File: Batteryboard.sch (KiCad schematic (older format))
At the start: 150 parts, among them IC1 FAN4010IL6X_F113, IC2 FAN4010IL6X_F113, IC3 FAN4010IL6X_F113, J1 Conn_01x02_Male, J2 Conn_01x03_Male, J3 Conn_01x05_Male, J4 Conn_01x02_Male, J5 SC_19-20, Q1 SI7617DN-T1-GE3, Q2 SI7617DN-T1-GE3, Q3 SI7617DN-T1-GE3, Q4 SIS412DN-T1-GE3, Q5 SIS412DN-T1-GE3, Q6 SIS412DN-T1-GE3, Q7 SI7617DN-T1-GE3, Q8 SIS412DN-T1-GE3, U1 BQ24617RGET, U2 TPS65279DAPR, U3 BQ29200DRBT, U4 PIC18F25K50-I_SO, U5 MCP2515-xSO, U6 SN65HVD1050D

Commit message: schematic is final now, working on routing my board again
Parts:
- C47: footprint Capacitor_SMD:C_0603_1608Metric -> Capacitor_SMD:C_0805_2012Metric
- IC1, IC2, IC3: symbol Batteryboard-rescue:FAN4010IL6X_F113-FAN4010IL6X_F113 -> FAN4010IL6X_F113:FAN4010IL6X_F113
- J1, J4: footprint Connector_JST:JST_VH_B2PS-VH_1x02_P3.96mm_Horizontal -> 1-1123723-2:1-1123723-2
- TMP1: symbol Batteryboard-rescue:LM50CIM3X-MASA-LIB -> MASA-LIB:LM50CIM3X
- U2: symbol Batteryboard-rescue:TPS65279DAPR-TPS65279DAPR -> TPS65279DAPR:TPS65279DAPR
- U4: symbol Batteryboard-rescue:PIC18F25K50-I_SO-PIC18F25K50-ISO -> PIC18F25K50-ISO:PIC18F25K50-I_SO
- gave numbers to parts that had none: 8
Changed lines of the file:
@@
 F 0 "J1" H 1308 4131 50  0000 C CNN
 F 1 "Conn_01x02_Male" H 1308 4040 50  0000 C CNN
-F 2 "Connector_JST:JST_VH_B2PS-VH_1x02_P3.96mm_Horizontal" H 1200 3950 50  0001 C CNN
+F 2 "1-1123723-2:1-1123723-2" H 1200 3950 50  0001 C CNN
 F 3 "~" H 1200 3950 50  0001 C CNN
 	1    1200 3950
@@
 F 0 "J4" H 10358 4781 50  0000 C CNN
 F 1 "Conn_01x02_Male" H 10358 4690 50  0000 C CNN
-F 2 "Connector_JST:JST_VH_B2PS-VH_1x02_P3.96mm_Horizontal" H 10250 4600 50  0001 C CNN
+F 2 "1-1123723-2:1-1123723-2" H 10250 4600 50  0001 C CNN
 F 3 "~" H 10250 4600 50  0001 C CNN
 	1    10250 4600
@@
 F 0 "C47" H 16115 7646 50  0000 L CNN
 F 1 "33uF" H 16115 7555 50  0000 L CNN
-F 2 "Capacitor_SMD:C_0603_1608Metric" H 16038 7450 50  0001 C CNN
+F 2 "Capacitor_SMD:C_0805_2012Metric" H 16038 7450 50  0001 C CNN
 F 3 "~" H 16000 7600 50  0001 C CNN
 	1    16000 7600
@@
 FB2
 $Comp
-L Batteryboard-rescue:FAN4010IL6X_F113-FAN4010IL6X_F113 IC2
+L FAN4010IL6X_F113:FAN4010IL6X_F113 IC2
 U 1 1 5E16FEE4
 P 11250 9300
@@
 	-1   0    0    -1
 $EndComp
-$Comp
-L Batteryboard-rescue:FAN4010IL6X_F113-FAN4010IL6X_F113 IC3
-U 1 1 5E16B258
-P 15800 8550
-F 0 "IC3" H 16350 8815 50  0000 C CNN
-F 1 "FAN4010IL6X_F113" H 16350 8724 50  0000 C CNN
-F 2 "MASA-LIB:6-LEAD_MICROPAK" H 16750 8650 50  0001 L CNN
-F 3 "http://pdl.designspark.com/api/v1/manufacturers/53f31bb99b4759f8698ebd6d/part/54f601839b4759c27e8ce92c/54f601849b4759c27e8ce954/1pdf" H 16750 8550 50  0001 L CNN
-F 4 "Current Sense Amplifier Single Single Ended 6-Pin MLP" H 16750 8450 50  0001 L CNN "Description"
-F 5 "" H 16750 8350 50  0001 L CNN "Height"
-F 6 "ON Semiconductor" H 16750 8250 50  0001 L CNN "Manufacturer_Name"
-F 7 "FAN4010IL6X_F113" H 16750 8150 50  0001 L CNN "Manufacturer_Part_Number"
-F 8 "512-FAN4010IL6X_F113" H 16750 8050 50  0001 L CNN "Mouser Part Number"
-F 9 "http://www.mouser.com/Search/ProductDetail.aspx?qs=bXpVsf6NmSLCEHlKPwERMg%3d%3d" H 16750 7950 50  0001 L CNN "Mouser Price/Stock"
-F 10 "8650874P" H 16750 7850 50  0001 L CNN "RS Part Number"
-F 11 "http://uk.rs-online.com/web/p/products/8650874P" H 16750 7750 50  0001 L CNN "RS Price/Stock"
-	1    15800 8550
-	1    0    0    -1
-$EndComp
 Text Notes 3950 8850 1    50   ~ 0
 make this guy give 3.6V so half the input
@@
 Wire Wire Line
 	12450 7900 12250 7900
-$Comp
-L Batteryboard-rescue:TPS65279DAPR-TPS65279DAPR U2
-U 1 1 5E217675
-P 12500 7000
-F 0 "U2" H 13400 7387 60  0000 C CNN
-F 1 "TPS65279DAPR" H 13400 7281 60  0000 C CNN
-F 2 "TPS65279DAPR:TPS65279DAPR" H 13400 7240 60  0001 C CNN
-F 3 "" H 12500 7000 60  0000 C CNN
-	1    12500 7000
-	1    0    0    -1
-$EndComp
 Wire Wire Line
 	13750 10050 13650 10050
@@
 	12500 7800 12450 7800
 $Comp
-L Batteryboard-rescue:LM50CIM3X-MASA-LIB TMP1
+L MASA-LIB:LM50CIM3X TMP1
 U 1 1 5E0BF102
 P 15000 9900
@@
 PGC
 $Comp
-L Batteryboard-rescue:PIC18F25K50-I_SO-PIC18F25K50-ISO U4
+L PIC18F25K50-ISO:PIC18F25K50-I_SO U4
 U 1 1 5EEDA796
 P 5000 8000
@@
 7.4V LINE
 $Comp
-L Batteryboard-rescue:FAN4010IL6X_F113-FAN4010IL6X_F113 IC1
-U 1 1 5E171494
-P 10100 1650
-F 0 "IC1" H 10650 1915 50  0000 C CNN
-F 1 "FAN4010IL6X_F113" H 10650 1824 50  0000 C CNN
-F 2 "MASA-LIB:6-LEAD_MICROPAK" H 11050 1750 50  0001 L CNN
-F 3 "http://pdl.designspark.com/api/v1/manufacturers/53f31bb99b4759f8698ebd6d/part/54f601839b4759c27e8ce92c/54f601849b4759c27e8ce954/1pdf" H 11050 1650 50  0001 L CNN
-F 4 "Current Sense Amplifier Single Single Ended 6-Pin MLP" H 11050 1550 50  0001 L CNN "Description"
-F 5 "" H 11050 1450 50  0001 L CNN "Height"
-F 6 "ON Semiconductor" H 11050 1350 50  0001 L CNN "Manufacturer_Name"
-F 7 "FAN4010IL6X_F113" H 11050 1250 50  0001 L CNN "Manufacturer_Part_Number"
-F 8 "512-FAN4010IL6X_F113" H 11050 1150 50  0001 L CNN "Mouser Part Number"
-F 9 "http://www.mouser.com/Search/ProductDetail.aspx?qs=bXpVsf6NmSLCEHlKPwERMg%3d%3d" H 11050 1050 50  0001 L CNN "Mouser Price/Stock"
-F 10 "8650874P" H 11050 950 50  0001 L CNN "RS Part Number"
-F 11 "http://uk.rs-online.com/web/p/products/8650874P" H 11050 850 50  0001 L CNN "RS Price/Stock"
-	1    10100 1650
-	1    0    0    1
-$EndComp
-$Comp
 L power:GNDREF #PWR0119
 U 1 1 5E267823
@@
 $EndComp
 $Comp
-L Device:C C?
+L Device:C C23
 U 1 1 5E428FCB
 P 14200 10050
-F 0 "C?" V 13948 10050 50  0000 C CNN
+F 0 "C23" V 13948 10050 50  0000 C CNN
 F 1 "1nF" V 14039 10050 50  0000 C CNN
 F 2 "Capacitor_SMD:C_0603_1608Metric" H 14238 9900 50  0001 C CNN
@@
 $EndComp
 $Comp
-L Device:C C?
+L Device:C C31
 U 1 1 5E429589
 P 14400 10050
-F 0 "C?" V 14148 10050 50  0000 C CNN
+F 0 "C31" V 14148 10050 50  0000 C CNN
 F 1 "100nF" V 14239 10050 50  0000 C CNN
 F 2 "Capacitor_SMD:C_0603_1608Metric" H 14438 9900 50  0001 C CNN
@@
 	14400 10200 14300 10200
 $Comp
-L power:GND #PWR?
+L power:GND #PWR01
 U 1 1 5E499F7C
 P 14300 10200
-F 0 "#PWR?" H 14300 9950 50  0001 C CNN
+F 0 "#PWR01" H 14300 9950 50  0001 C CNN
 F 1 "GND" H 14305 10027 50  0000 C CNN
 F 2 "" H 14300 10200 50  0001 C CNN
@@
 	14300 10200 14200 10200
 $Comp
-L Device:C C?
+L Device:C C45
 U 1 1 5E49A4E1
 P 15550 10050
-F 0 "C?" V 15298 10050 50  0000 C CNN
+F 0 "C45" V 15298 10050 50  0000 C CNN
 F 1 "1nF" V 15389 10050 50  0000 C CNN
 F 2 "Capacitor_SMD:C_0603_1608Metric" H 15588 9900 50  0001 C CNN
@@
 $EndComp
 $Comp
-L Device:C C?
+L Device:C C46
 U 1 1 5E49ACDA
 P 15950 10050
-F 0 "C?" V 15698 10050 50  0000 C CNN
+F 0 "C46" V 15698 10050 50  0000 C CNN
 F 1 "100nF" V 15789 10050 50  0000 C CNN
 F 2 "Capacitor_SMD:C_0603_1608Metric" H 15988 9900 50  0001 C CNN
@@
 $EndComp
 $Comp
-L Device:C C?
+L Device:C C48
 U 1 1 5E49AFF1
 P 16600 10050
-F 0 "C?" V 16348 10050 50  0000 C CNN
+F 0 "C48" V 16348 10050 50  0000 C CNN
 F 1 "100nF" V 16439 10050 50  0000 C CNN
 F 2 "Capacitor_SMD:C_0603_1608Metric" H 16638 9900 50  0001 C CNN
@@
 $EndComp
 $Comp
-L Device:C C?
+L Device:C C49
 U 1 1 5E49B600
 P 17050 10050
-F 0 "C?" V 16798 10050 50  0000 C CNN
+F 0 "C49" V 16798 10050 50  0000 C CNN
 F 1 "2.2uF" V 16889 10050 50  0000 C CNN
 F 2 "Capacitor_SMD:C_0603_1608Metric" H 17088 9900 50  0001 C CNN
@@
 $EndComp
 $Comp
-L Device:R_US R?
+L Device:R_US R46
 U 1 1 5E49BA5F
 P 16850 10300
-F 0 "R?" H 16918 10346 50  0000 L CNN
+F 0 "R46" H 16918 10346 50  0000 L CNN
 F 1 "3.3Ohm" H 16918 10255 50  0000 L CNN
 F 2 "Resistor_SMD:R_0603_1608Metric" V 16890 10290 50  0001 C CNN
@@
 $EndComp
 $Comp
-L Device:L L?
+L Device:L L4
 U 1 1 5E49C1EF
 P 16300 9900
-F 0 "L?" V 16490 9900 50  0000 C CNN
+F 0 "L4" V 16490 9900 50  0000 C CNN
 F 1 "2.2uH" V 16399 9900 50  0000 C CNN
 F 2 "Inductor_SMD:L_0603_1608Metric" H 16300 9900 50  0001 C CNN
@@
 	15950 10200 15750 10200
 $Comp
-L power:GND #PWR?
+L power:GND #PWR02
 U 1 1 5E5BCE71
 P 15750 10200
-F 0 "#PWR?" H 15750 9950 50  0001 C CNN
+F 0 "#PWR02" H 15750 9950 50  0001 C CNN
 F 1 "GND" H 15755 10027 50  0000 C CNN
 F 2 "" H 15750 10200 50  0001 C CNN
@@
 	15750 10200 15550 10200
 $Comp
-L power:GND #PWR?
+L power:GND #PWR03
 U 1 1 5E5BD350
 P 16600 10300
-F 0 "#PWR?" H 16600 10050 50  0001 C CNN
+F 0 "#PWR03" H 16600 10050 50  0001 C CNN
 F 1 "GND" H 16605 10127 50  0000 C CNN
 F 2 "" H 16600 10300 50  0001 C CNN
@@
 $EndComp
 Connection ~ 16600 10300
+$Comp
+L TPS65279DAPR:TPS65279DAPR U2
+U 1 1 5E217675
+P 12500 7000
+F 0 "U2" H 13400 7387 60  0000 C CNN
+F 1 "TPS65279DAPR" H 13400 7281 60  0000 C CNN
+F 2 "TPS65279DAPR:TPS65279DAPR" H 13400 7240 60  0001 C CNN
+F 3 "" H 12500 7000 60  0000 C CNN
+	1    12500 7000
+	1    0    0    -1
+$EndComp
+$Comp
+L FAN4010IL6X_F113:FAN4010IL6X_F113 IC3
+U 1 1 5E16B258
+P 15800 8550
+F 0 "IC3" H 16350 8815 50  0000 C CNN
+F 1 "FAN4010IL6X_F113" H 16350 8724 50  0000 C CNN
+F 2 "MASA-LIB:6-LEAD_MICROPAK" H 16750 8650 50  0001 L CNN
+F 3 "http://pdl.designspark.com/api/v1/manufacturers/53f31bb99b4759f8698ebd6d/part/54f601839b4759c27e8ce92c/54f601849b4759c27e8ce954/1pdf" H 16750 8550 50  0001 L CNN
+F 4 "Current Sense Amplifier Single Single Ended 6-Pin MLP" H 16750 8450 50  0001 L CNN "Description"
+F 5 "" H 16750 8350 50  0001 L CNN "Height"
+F 6 "ON Semiconductor" H 16750 8250 50  0001 L CNN "Manufacturer_Name"
+F 7 "FAN4010IL6X_F113" H 16750 8150 50  0001 L CNN "Manufacturer_Part_Number"
+F 8 "512-FAN4010IL6X_F113" H 16750 8050 50  0001 L CNN "Mouser Part Number"
+F 9 "http://www.mouser.com/Search/ProductDetail.aspx?qs=bXpVsf6NmSLCEHlKPwERMg%3d%3d" H 16750 7950 50  0001 L CNN "Mouser Price/Stock"
+F 10 "8650874P" H 16750 7850 50  0001 L CNN "RS Part Number"
+F 11 "http://uk.rs-online.com/web/p/products/8650874P" H 16750 7750 50  0001 L CNN "RS Price/Stock"
+	1    15800 8550
+	1    0    0    -1
+$EndComp
+$Comp
+L FAN4010IL6X_F113:FAN4010IL6X_F113 IC1
+U 1 1 5E171494
+P 10100 1650
+F 0 "IC1" H 10650 1915 50  0000 C CNN
+F 1 "FAN4010IL6X_F113" H 10650 1824 50  0000 C CNN
+F 2 "MASA-LIB:6-LEAD_MICROPAK" H 11050 1750 50  0001 L CNN
+F 3 "http://pdl.designspark.com/api/v1/manufacturers/53f31bb99b4759f8698ebd6d/part/54f601839b4759c27e8ce92c/54f601849b4759c27e8ce954/1pdf" H 11050 1650 50  0001 L CNN
+F 4 "Current Sense Amplifier Single Single Ended 6-Pin MLP" H 11050 1550 50  0001 L CNN "Description"
+F 5 "" H 11050 1450 50  0001 L CNN "Height"
+F 6 "ON Semiconductor" H 11050 1350 50  0001 L CNN "Manufacturer_Name"
+F 7 "FAN4010IL6X_F113" H 11050 1250 50  0001 L CNN "Manufacturer_Part_Number"
+F 8 "512-FAN4010IL6X_F113" H 11050 1150 50  0001 L CNN "Mouser Part Number"
+F 9 "http://www.mouser.com/Search/ProductDetail.aspx?qs=bXpVsf6NmSLCEHlKPwERMg%3d%3d" H 11050 1050 50  0001 L CNN "Mouser Price/Stock"
+F 10 "8650874P" H 11050 950 50  0001 L CNN "RS Part Number"
+F 11 "http://uk.rs-online.com/web/p/products/8650874P" H 11050 850 50  0001 L CNN "RS Price/Stock"
+	1    10100 1650
+	1    0    0    1
+$EndComp
 $EndSCHEMATC

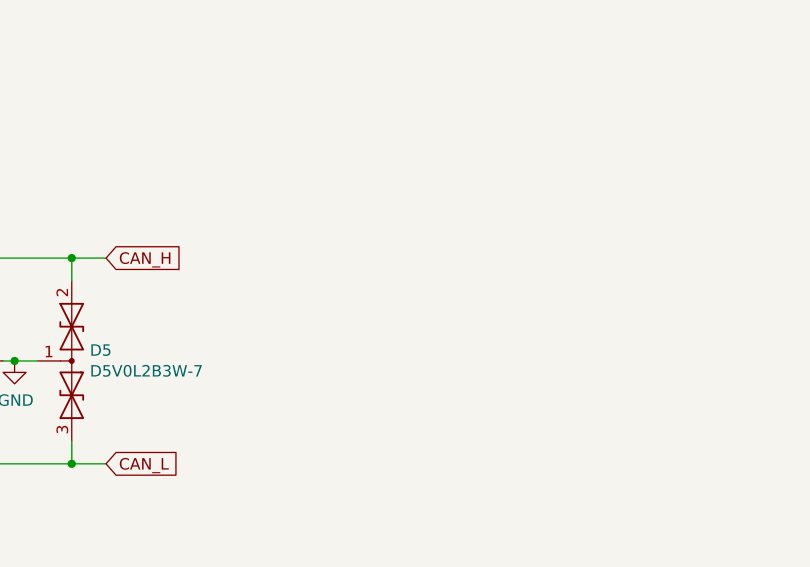
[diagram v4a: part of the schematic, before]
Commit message: added 4 pin for AOA sensor
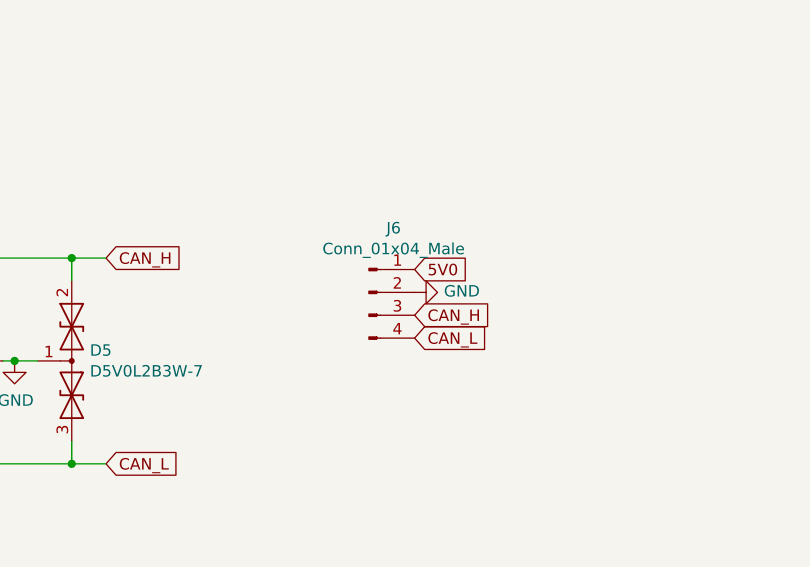
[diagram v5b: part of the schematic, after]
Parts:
- added J6: Conn_01x04_Male, 5013310407:1734595-4, symbol Connector:Conn_01x04_Male
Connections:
- net 5V0: now also J6.1 (Pin_1)
- net CAN_H: now also J6.3 (Pin_3)
- net CAN_L: now also J6.4 (Pin_4)
- net GND: now also J6.2 (Pin_2)
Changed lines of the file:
@@
 	1    0    0    1
 $EndComp
+$Comp
+L Connector:Conn_01x04_Male J6
+U 1 1 5E406AAF
+P 6850 11050
+F 0 "J6" H 6958 11331 50  0000 C CNN
+F 1 "Conn_01x04_Male" H 6958 11240 50  0000 C CNN
+F 2 "5013310407:1734595-4" H 6850 11050 50  0001 C CNN
+F 3 "~" H 6850 11050 50  0001 C CNN
+	1    6850 11050
+	1    0    0    -1
+$EndComp
+$Comp
+L power:GND #PWR0107
+U 1 1 5E531ADE
+P 7050 11050
+F 0 "#PWR0107" H 7050 10800 50  0001 C CNN
+F 1 "GND" V 7055 10922 50  0000 R CNN
+F 2 "" H 7050 11050 50  0001 C CNN
+F 3 "" H 7050 11050 50  0001 C CNN
+	1    7050 11050
+	0    -1   -1   0
+$EndComp
+Text GLabel 7050 10950 2    50   Input ~ 0
+5V0
+Text GLabel 7050 11150 2    50   Input ~ 0
+CAN_H
+Text GLabel 7050 11250 2    50   Input ~ 0
+CAN_L
 $EndSCHEMATC

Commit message: made lots of progress on silkscreen, and fixed some jank with values
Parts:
- added Z1, Z11, Z12, Z14, Z15, Z16, Z19, Z20, Z21, Z22, Z23, Z3, Z4, Z5, Z6, Z9: TESTPOINT, TESTPOINT:TESTPOINT, symbol TESTPOINT:TESTPOINT
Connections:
- net 3V3: now also Z14.1
- net 5V0: now also Z9.1
- net GND: now also Z5.1
- net GNDREF: now also Z4.1
- net Q4D: now also Z6.1
- net Q6G: now also Z21.1
- net SRN: now also Z16.1
- net TEMP_OUT: now also Z15.1
- net VBAT: now also Z19.1
- net at J1.1 (Pin_1), Q1.5 (D_1), Q1.6 (D_2)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: now also Z1.1
- net at NTCTH1/NTCG163JF103FT1S1.2, R10/RT1.2, R16.2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: now also Z3.1
- net at CIN1.1, RIN1.1, U3.1 (VC2): now also Z22.1
- net at CIN1.2, CIN2.1, RIN2.1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: now also Z20.1
- net at C45.2, C46.2, L4.1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: now also Z12.1
- net at C47.1, IC3.1 (VIN), L3.2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: now also Z23.1
- net at C44.2, IC2.1 (VIN), L2.1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: now also Z11.1
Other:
- moved on the sheet: C30, CCD1, R30, R31, R_JUMP1

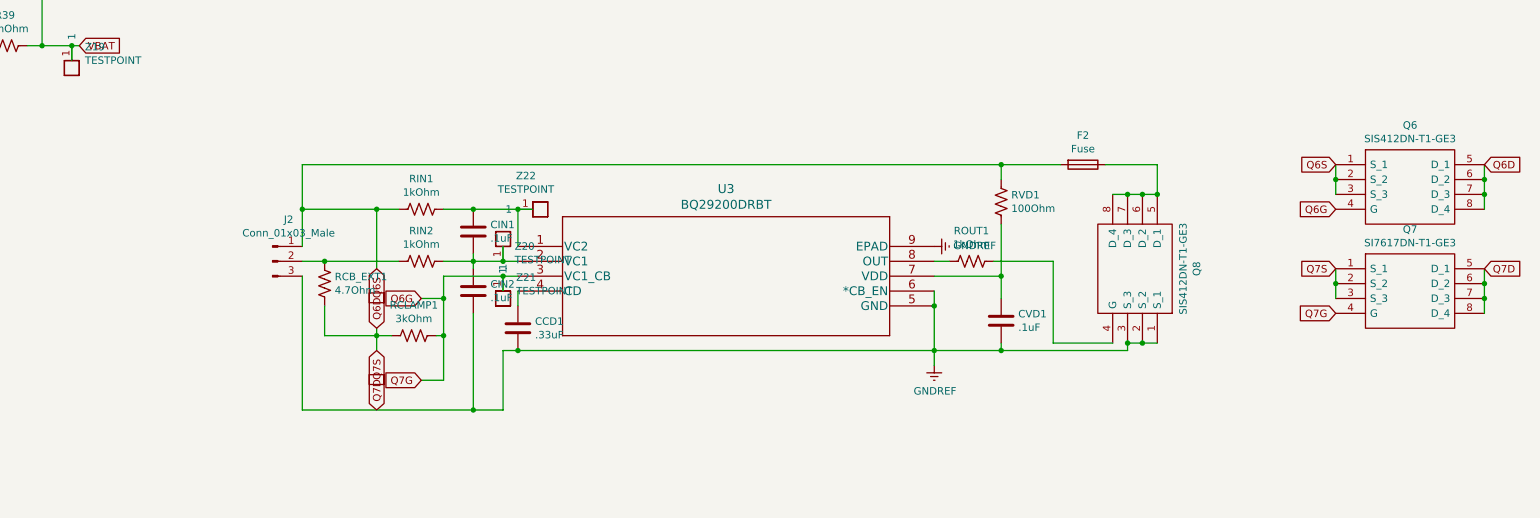
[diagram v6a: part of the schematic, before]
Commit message: changed up balancing circuit cuz that no work and that bad
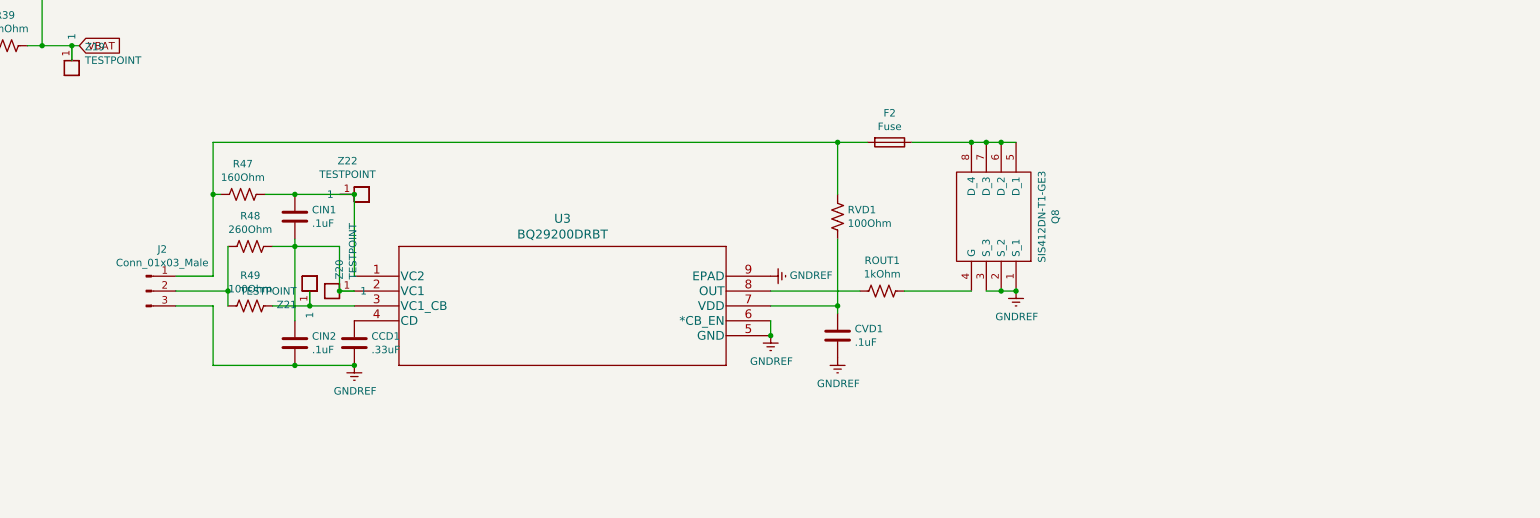
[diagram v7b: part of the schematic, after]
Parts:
- removed Q6: SIS412DN-T1-GE3, SI7617DN-T1-GE3:SIS862DNT1GE3, symbol Batteryboard-rescue:SI7617DN-T1-GE3-SI7617DN-T1-GE3
- removed Q7: SI7617DN-T1-GE3, SI7617DN-T1-GE3:SIS862DNT1GE3, symbol Batteryboard-rescue:SI7617DN-T1-GE3-SI7617DN-T1-GE3
- removed RCB_EXT1: 4.7Ohm, Resistor_SMD:R_0603_1608Metric, symbol Device:R_US
- removed RCLAMP1: 3kOhm, Resistor_SMD:R_0603_1608Metric, symbol Device:R_US
- removed RIN1, RIN2: 1kOhm, Resistor_SMD:R_0603_1608Metric, symbol Device:R_US
- added R47: 160Ohm, Resistor_SMD:R_0603_1608Metric, symbol Device:R_US
- added R48: 260Ohm, Resistor_SMD:R_0603_1608Metric, symbol Device:R_US
- added R49: 100Ohm, Resistor_SMD:R_0603_1608Metric, symbol Device:R_US
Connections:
- net at CIN1.1, U3.1 (VC2), Z22.1: now also R47.1
- net at CIN1.2, CIN2.1, U3.2 (VC1)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: now also R48.1
- net at J2.2 (Pin_2): now also R48.2, R49.2
- net Q6G: no longer names the net of U3.3 (VC1_CB), Z21.1
- net Q6G: now also R49.1
- net Q6S: no longer names the net of F2.2, J2.1 (Pin_1), RVD1.1
- net Q6S: now also R47.2
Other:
- moved on the sheet: CCD1, CIN1, CIN2, CVD1, F2, J2, Q8, ROUT1, RVD1, U3, Z20, Z21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

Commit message: made some finishing touches, should be complete now
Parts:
- R48: value 260Ohm -> 261Ohm
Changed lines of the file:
@@
 P 12300 3950
 F 0 "R48" V 12095 3950 50  0000 C CNN
-F 1 "260Ohm" V 12186 3950 50  0000 C CNN
+F 1 "261Ohm" V 12186 3950 50  0000 C CNN
 F 2 "Resistor_SMD:R_0603_1608Metric" V 12340 3940 50  0001 C CNN
 F 3 "~" H 12300 3950 50  0001 C CNN
